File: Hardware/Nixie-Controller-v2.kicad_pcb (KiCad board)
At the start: 4 copper layers, 220 x 65 mm, 228 parts, among them J7 12V DC JACK, U1 MAX1771, U10 74HC4067, U11 M41T01, U12 STM32F103C8, U13 OPA180, U14 74HC4067, U15 OPA180, U16 74HC4067, U17 OPA180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

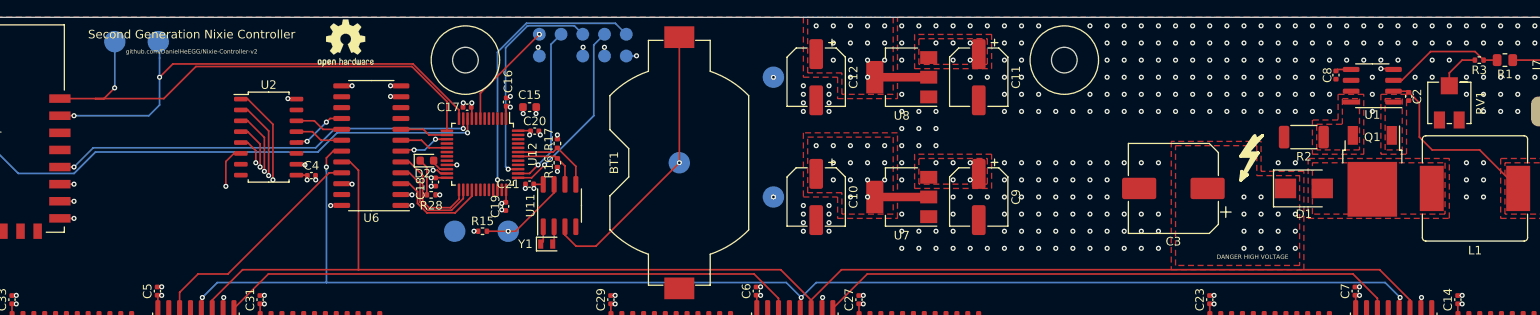
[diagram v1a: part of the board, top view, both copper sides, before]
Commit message: Increase silkscreen text size
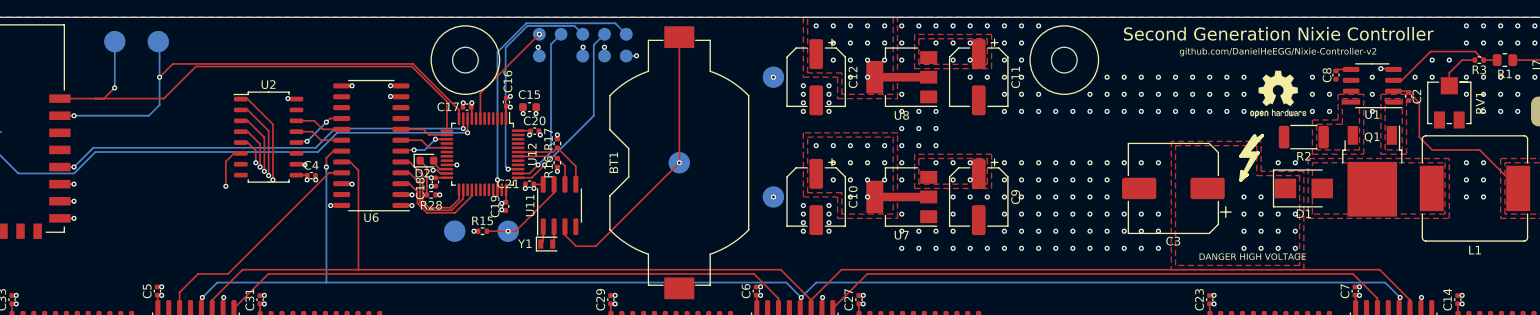
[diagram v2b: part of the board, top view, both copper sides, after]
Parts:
- moved REF** 109.2 mm to (219.0, 67.0)
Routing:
- net GND: vias 437 -> 367

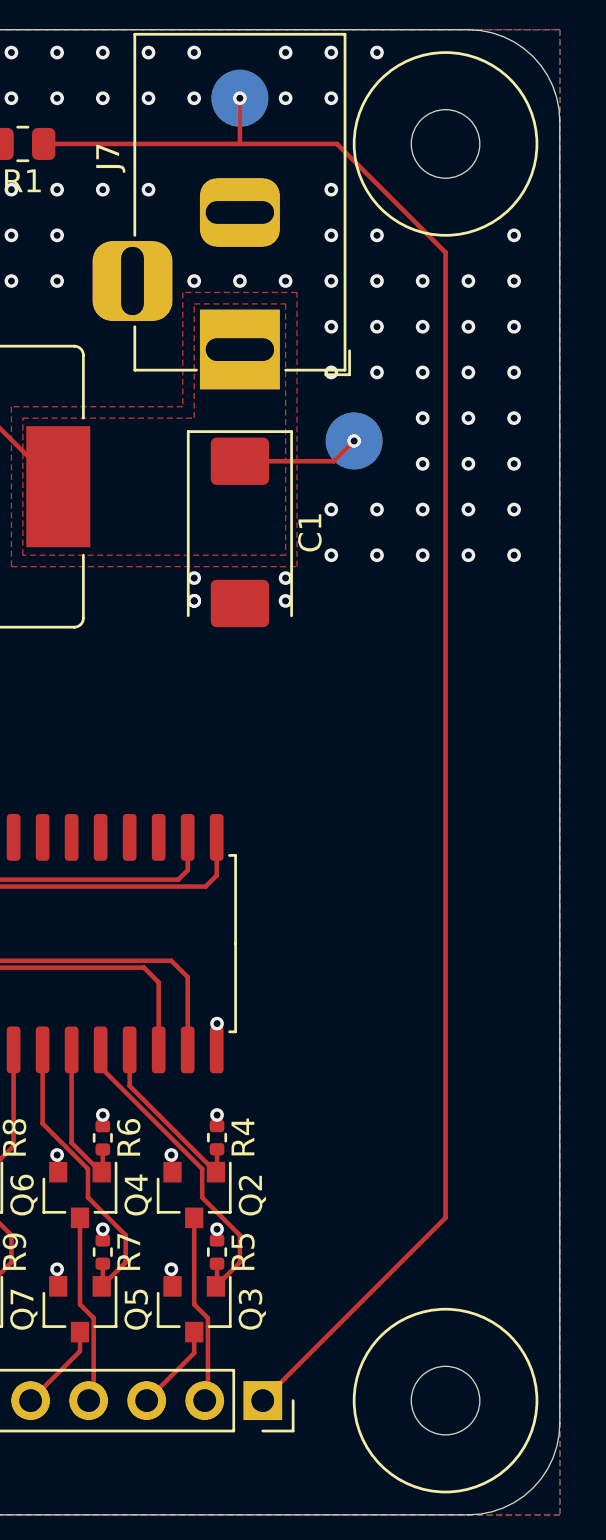
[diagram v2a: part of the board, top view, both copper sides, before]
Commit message: Shift HV kelvin line to prevent shorts
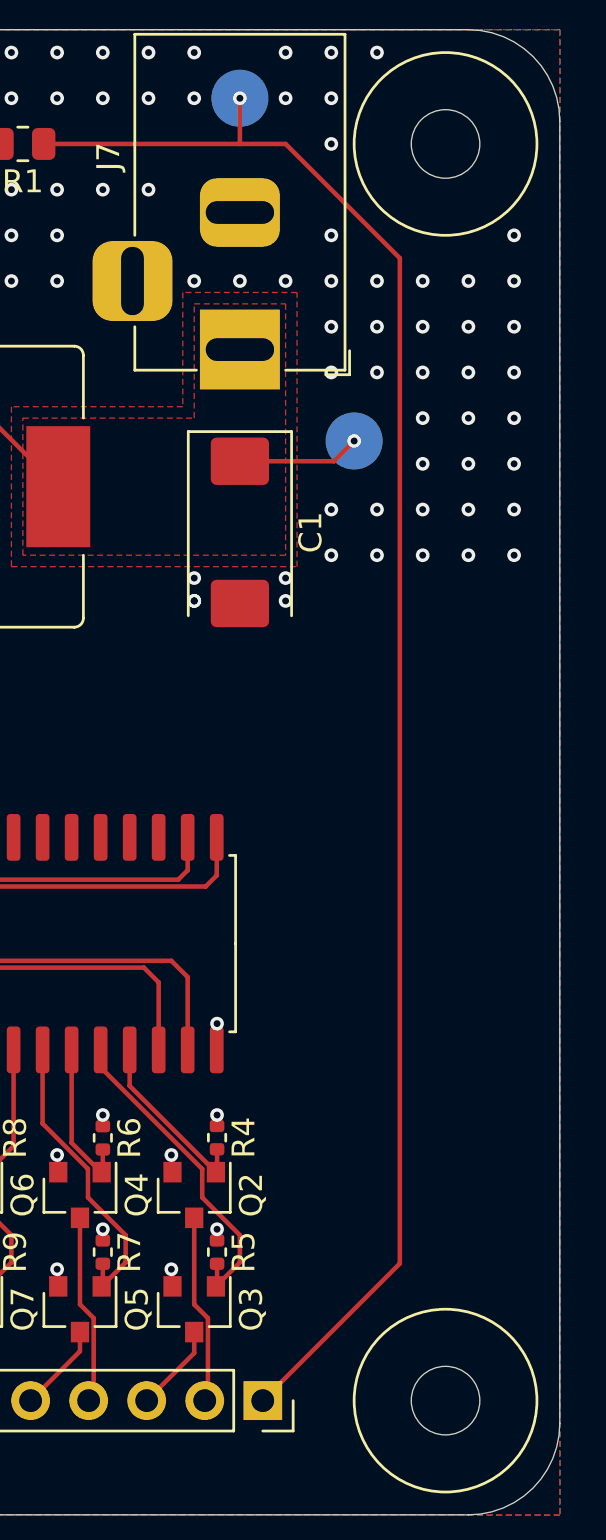
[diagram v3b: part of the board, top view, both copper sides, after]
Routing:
- net +HV: track 75.1 -> 72.1 mm
- net GND: vias 367 -> 366

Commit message: Remove status LED
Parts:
- removed D2: LED, Diode_SMD:D_0603_1608Metric
- removed R28: 100, Resistor_SMD:R_0402_1005Metric
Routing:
- net Net-(D2-Pad1): track 4.32 -> 0.00 mm
- net Net-(U12-Pad22): track 2.12 -> 0.00 mm
- net GND: track 72.1 -> 71.6 mm, vias 366 -> 365

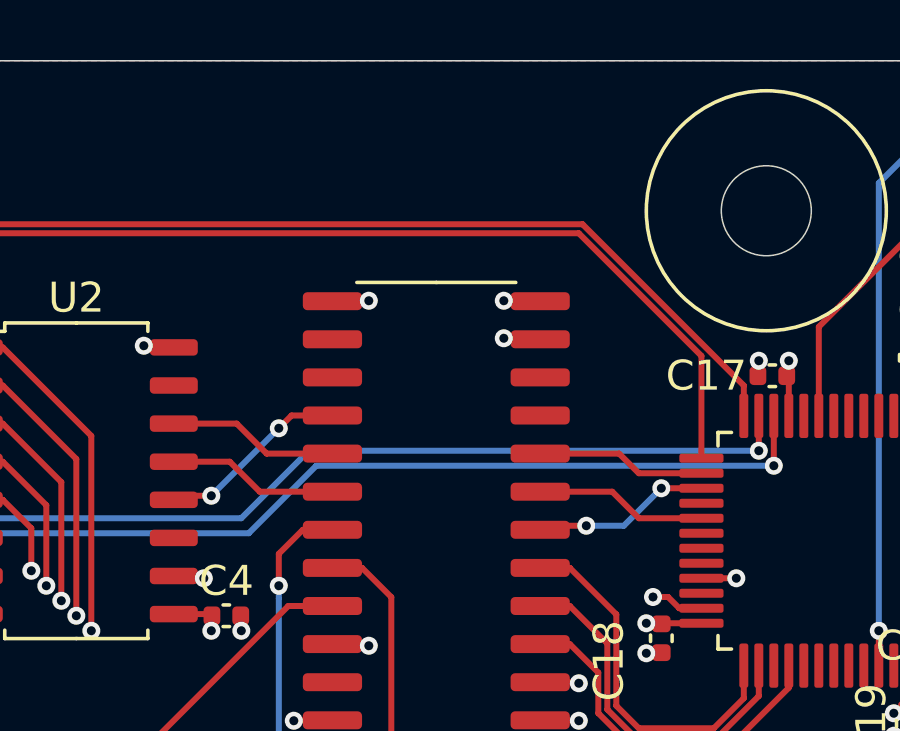
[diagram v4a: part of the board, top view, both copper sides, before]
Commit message: Add reset jumper
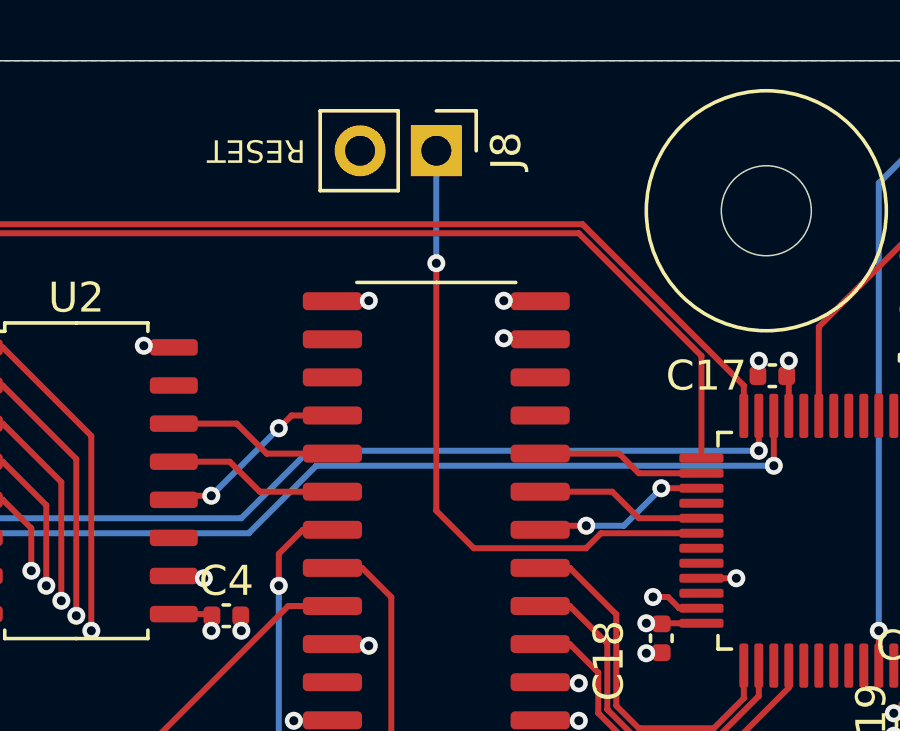
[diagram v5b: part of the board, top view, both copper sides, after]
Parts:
- added J8: RST, Connector_PinHeader_2.54mm:PinHeader_1x02_P2.54mm_Vertical, F.Cu at (113.0, 61.0)
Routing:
- net Net-(J8-Pad1): track 0.00 -> 21.6 mm, vias 0 -> 1
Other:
- board text added: "RESET"

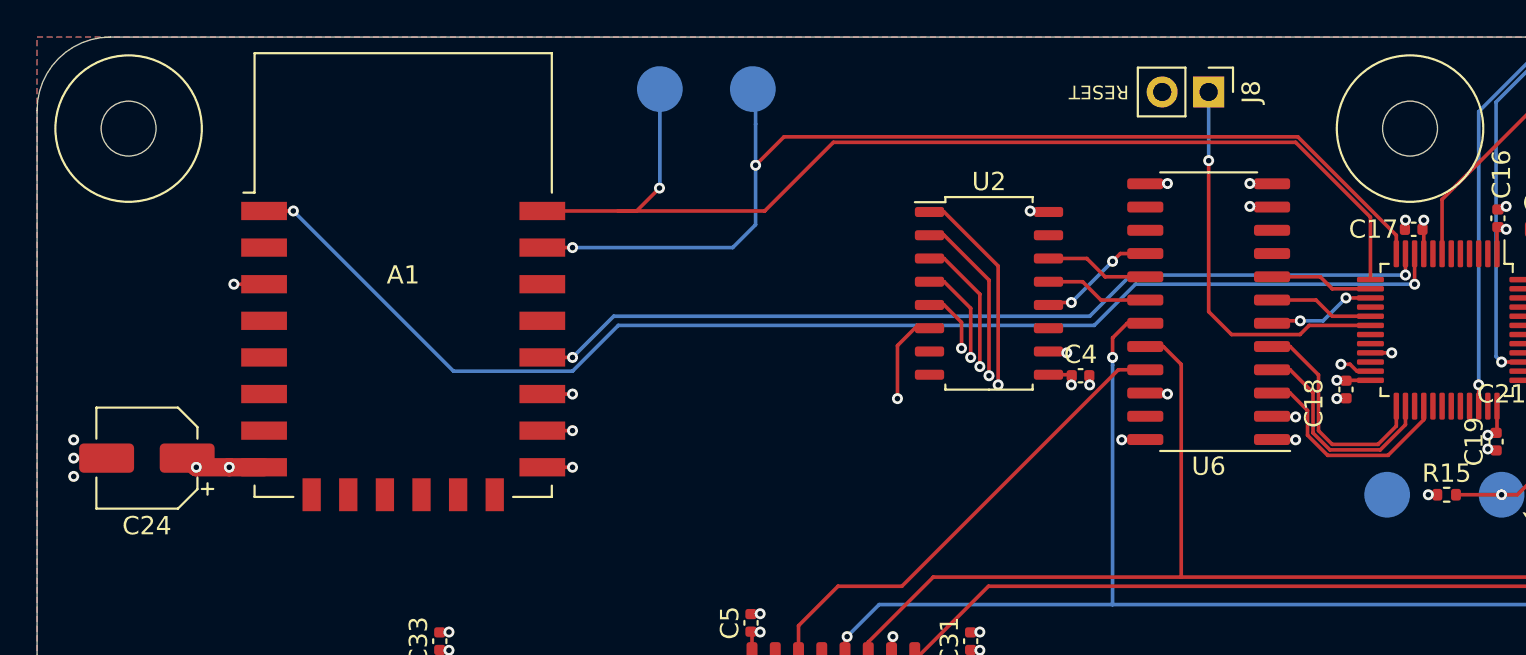
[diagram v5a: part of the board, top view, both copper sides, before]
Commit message: Switch to ESP32-WROOM-32E wifi module
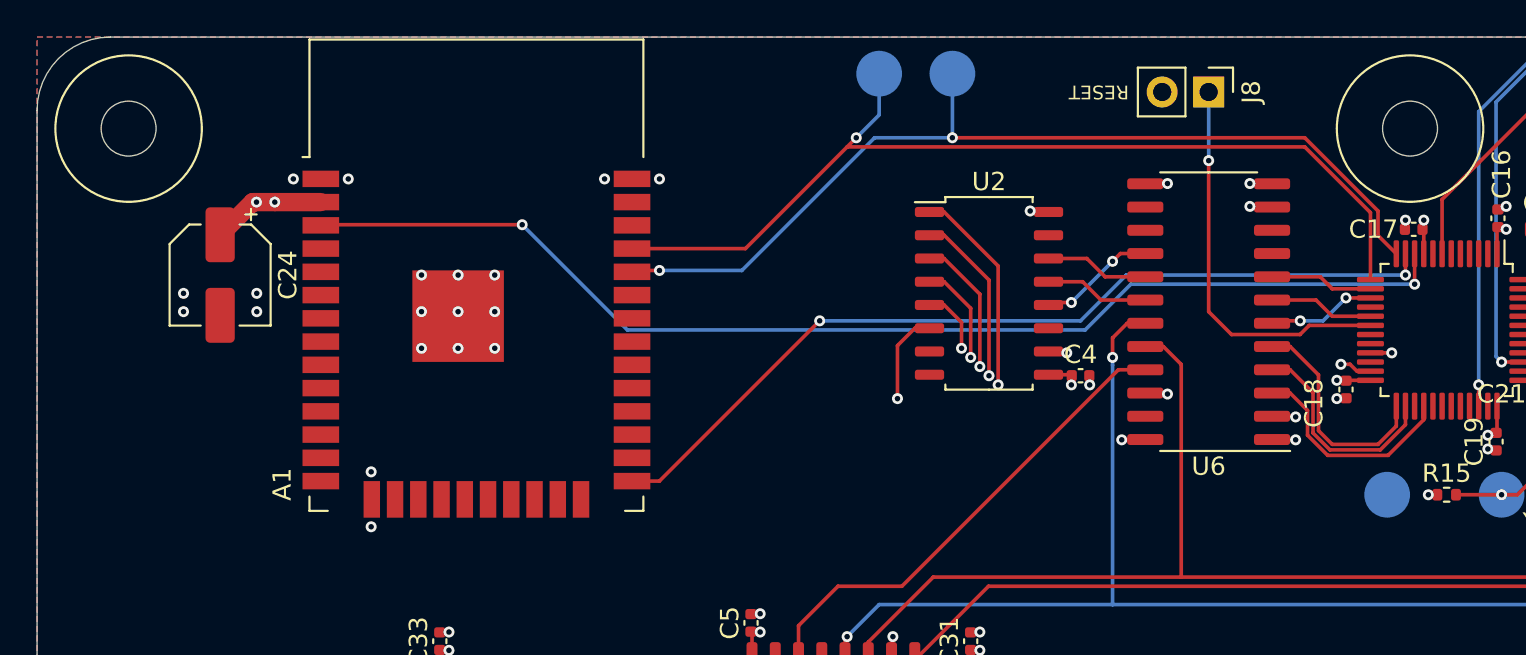
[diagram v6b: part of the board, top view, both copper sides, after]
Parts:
- A1: value ESP-12F -> ESP32-WROOM-32E; footprint RF_Module:ESP-12E -> RF_Module:ESP32-WROOM-32
- moved TP17 12.0 mm to (95.0, 60.0)
- moved TP18 10.9 mm to (99.0, 60.0)
- moved C24 10.8 mm to (59.0, 71.0), turned to 270 degrees
- moved A1 5.00 mm to (73.0, 74.0)
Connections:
- A1 pad 1: ESP_nRST -> GND
- A1 pad 16: GND -> Net-(A1-Pad16)
- A1 pad 17: +3V3 -> Net-(A1-Pad17)
- A1 pad 18: ESP_RUN -> Net-(A1-Pad18)
- A1 pad 2: Net-(A1-Pad2) -> +3V3
- A1 pad 21: ESP_TX -> Net-(A1-Pad21)
- A1 pad 22: ESP_RX -> Net-(A1-Pad22)
- A1 pad 3: +3V3 -> ESP_nRST
- A1 pad 8: +3V3 -> Net-(A1-Pad8)
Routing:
- net ESP_RX: track 60.1 -> 52.5 mm
- net ESP_TX: track 58.5 -> 51.7 mm
- net ESP_nRST: track 70.1 -> 64.8 mm
- net GND: track 71.6 -> 68.3 mm, vias 365 -> 379
- net ESP_RUN: track 50.2 -> 48.1 mm
- net +3V3: track 31.4 -> 30.0 mm, vias 33 -> 31
